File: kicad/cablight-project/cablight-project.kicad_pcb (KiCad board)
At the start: 2 copper layers, 150 x 42 mm, 20 parts, among them J1 Screw_Term_1x2_2.54mm, J2 Screw_Term_1x2_2.54mm, M3 MountingHole_3.2mm_M3_ISO1458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, P1 POLOLU D24V10F5, Q1 IRLB8721PBF, SW1 PEC11, SW3 switch_SPDT_SLW_121586

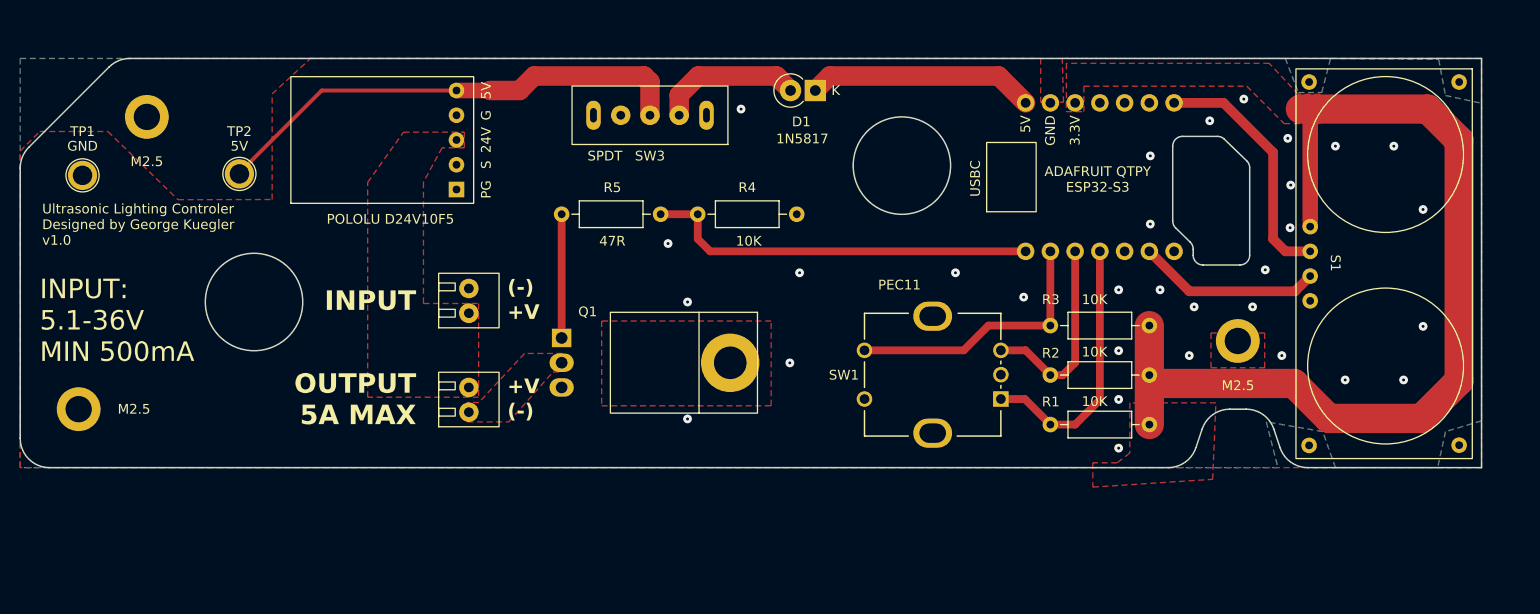
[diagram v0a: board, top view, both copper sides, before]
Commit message: Add Button code support and make ultrasonic notify from task.
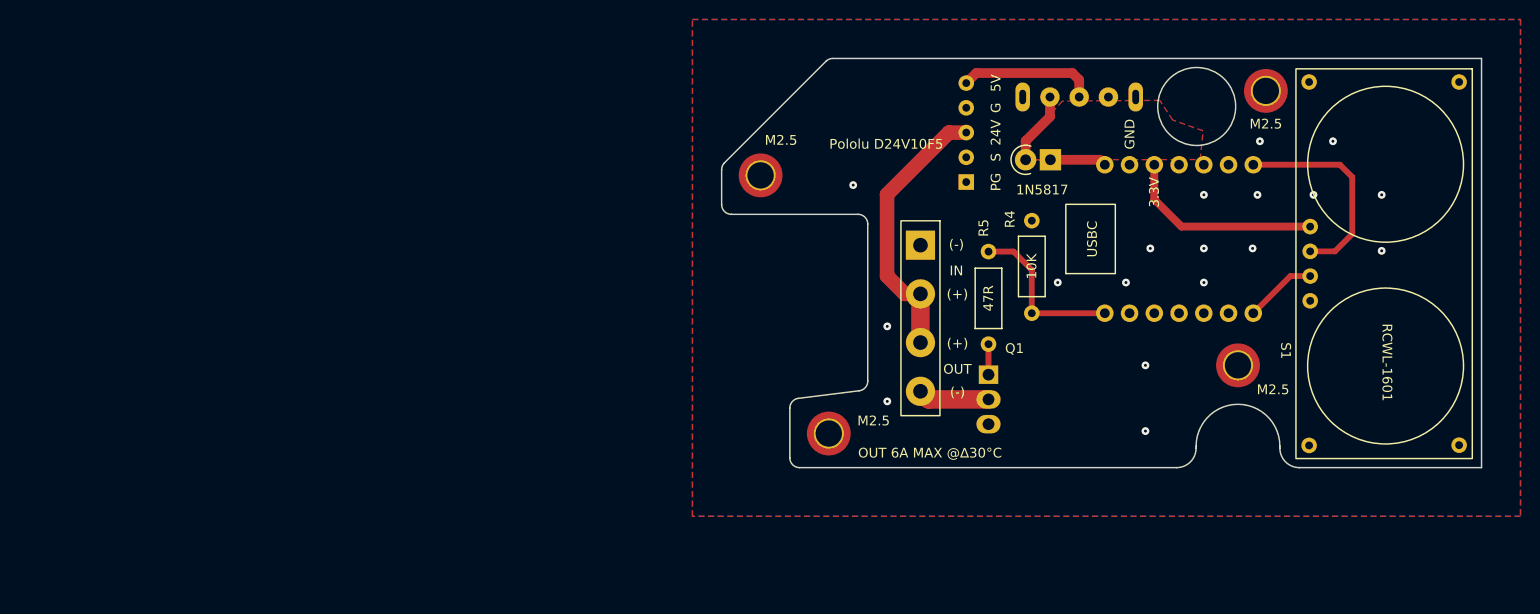
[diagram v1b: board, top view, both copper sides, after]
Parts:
- removed J1, J2: Screw_Term_1x2_2.54mm, user:2xTermBlock_254mm
- removed M3: MountingHole_3.2mm_M3_ISO14580_Pad_TopOnly, user:MountingHole_3.2mm_M3_ISO14580_Pad_TopOnly
- removed R1, R2, R3: 10K, Resistor_THT:R_Axial_DIN0207_L6.3mm_D2.5mm_P10.16mm_Horizontal
- removed REF** (x3): MountingHole_2.7mm_M2.5_ISO7380_Pad_Heated_Insert, user:MountingHole_2.7mm_M2.5_ISO7380_Pad_Heated_Insert
- removed SW1: PEC11, user:Bourns-PEC11R
- removed TP1: GND, TestPoint:TestPoint_Plated_Hole_D2.0mm
- removed TP2: 5V, TestPoint:TestPoint_Plated_Hole_D2.0mm
- added J3: Screw_Term_1x4_5mm, GRK_Lib:Molex 4pin Terminal Block, F.Cu at (-57.6, 19.2)
- added M2.5: MountingHole_2.7mm_M2.5_ISO7380_Pad_TopOnly, MountingHole:MountingHole_2.7mm_M2.5_ISO7380_Pad_TopOnly, F.Cu at (-67.0, 38.5)
- added M2.5: MountingHole_2.7mm_M2.5_ISO7380_Pad_TopOnly, MountingHole:MountingHole_2.7mm_M2.5_ISO7380_Pad_TopOnly, F.Cu at (-25.0, 31.5)
- added M2.5: MountingHole_2.7mm_M2.5_ISO7380_Pad_TopOnly, MountingHole:MountingHole_2.7mm_M2.5_ISO7380_Pad_TopOnly, F.Cu at (-74.0, 12.0)
- added M2.5: MountingHole_2.7mm_M2.5_ISO7380_Pad_TopOnly, MountingHole:MountingHole_2.7mm_M2.5_ISO7380_Pad_TopOnly, F.Cu at (-22.1, 3.33)
- D1: footprint Diode_THT:D_DO-41_SOD81_P2.54mm_Vertical_KathodeUp -> GRK_Lib:D_DO-41_SOD81_P2.54mm_Vertical_KathodeUp
- P1: value POLOLU D24V10F5 -> Pololu D24V10F5; footprint user:Pololu_5V_H -> GRK_Lib:Pololu_5V_H
- Q1: footprint user:TO-220F-3_H_Heatsink -> GRK_Lib:TO-220F-3_H_Heatsink
- R4, R5: footprint Resistor_THT:R_Axial_DIN0207_L6.3mm_D2.5mm_P10.16mm_Horizontal -> GRK_Lib:R_Axial_DIN0207_L6.3mm_D2.5mm_P9.5mm
- S1: footprint user:RCWL-1601 -> GRK_Lib:RCWL-1601
- SW3: footprint user:CUI_SPDT_500mA_3mm -> GRK_Lib:Switch_SPDT_CUI_500mA_3mm
- U1: footprint user:AdafruitQTPyEsp32S3 -> GRK_Lib:AdafruitQTPyEsp32S3
- moved P1 52.3 mm to (-52.9, 7.61)
- moved SW3 44.1 mm to (-41.3, 3.96), turned to 0 degrees
- moved Q1 44.0 mm to (-50.6, 32.5)
- moved R4 35.8 mm to (-46.2, 26.1), turned to 90 degrees
- moved R5 33.9 mm to (-50.6, 19.8), turned to -90 degrees
- moved D1 25.2 mm to (-44.3, 10.4)
- moved U1 10.3 mm to (-38.7, 26.1)
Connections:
- net /+3V3 renamed /SRO4 PWR
- net /+5V_MCU renamed /5V_MCU
- net /+5V_SW renamed /5V_sw
- net Net-(S1-Trig) renamed /trig
- S1 pad 3: Net-(S1-Echo) -> /echo
- U1 pad 2: Net-(SW1-S2) -> unconnected-(U1-GPIO_17-Pad2)
- U1 pad 3: Net-(U1-GPIO_9) -> unconnected-(U1-GPIO_9-Pad3)
- U1 pad 4: Net-(U1-GPIO_8) -> unconnected-(U1-GPIO_8-Pad4)
- U1 pad 6: Net-(S1-Echo) -> unconnected-(U1-GPIO_6-Pad6)
- U1 pad 7: unconnected-(U1-GPIO_5-Pad7) -> /echo
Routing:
- net /SRO4 PWR: track 99.8 -> 20.7 mm
- net /+5V: track 50.1 -> 14.1 mm
- net /+24V: track 0.01 -> 28.3 mm
- net Net-(SW1-S2): track 27.8 -> 0.00 mm
- net Net-(U1-GPIO_8): track 27.5 -> 0.00 mm
- net Net-(U1-GPIO_18): track 40.5 -> 17.2 mm
- net Net-(U1-GPIO_9): track 20.6 -> 0.00 mm
- net Net-(S1-Echo): track 18.9 -> 0.00 mm
- net /5V_MCU: track 23.4 -> 5.80 mm
- net Net-(Q1-G): track 12.7 -> 3.14 mm
- net /5V_sw: track 15.0 -> 7.48 mm
- net /echo: track 0.00 -> 7.42 mm
- net /LED-: track 0.00 -> 7.33 mm
- net /trig: track 25.6 -> 21.6 mm
- net <NO NET>: vias 31 -> 18
- removed copper zone on F.Cu, net /+24V
- removed copper zone on F.Cu, net /LED-
- removed copper zone on F.Cu, net /SRO4 PWR
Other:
- board size 150 x 42 mm -> 78 x 42 mm
- board text added: "(+)"
- board text added: "- Need to confirm my dimensions on the ultrasonic ended up corrent or if I need to adjust tolerences due to soldering error. - Need to attempt to install my M2.5 bosses."
- board text added: "IN"
- board text added: "OUT"
- board text added: "OUT 6A MAX @∆30°C"
- board text added: "Ultrasonic Lighting Controler Designed by George R. Kuegler v2.0 - 2025-07-07 Haverhill, MA"
- board text removed: "+V"
- board text removed: "ADAFRUIT QTPY ESP32-S3"
- board text removed: "Hole for Case Mount"
- board text removed: "INPUT"
- board text removed: "INPUT: 5.1-36V MIN 500mA"
- board text removed: "JLCJLCJLCJLCJLC"
- board text removed: "OUTPUT 5A MAX"
- board text removed: "Ultrasonic Lighting Controler Designed by George Kuegler v1.0"

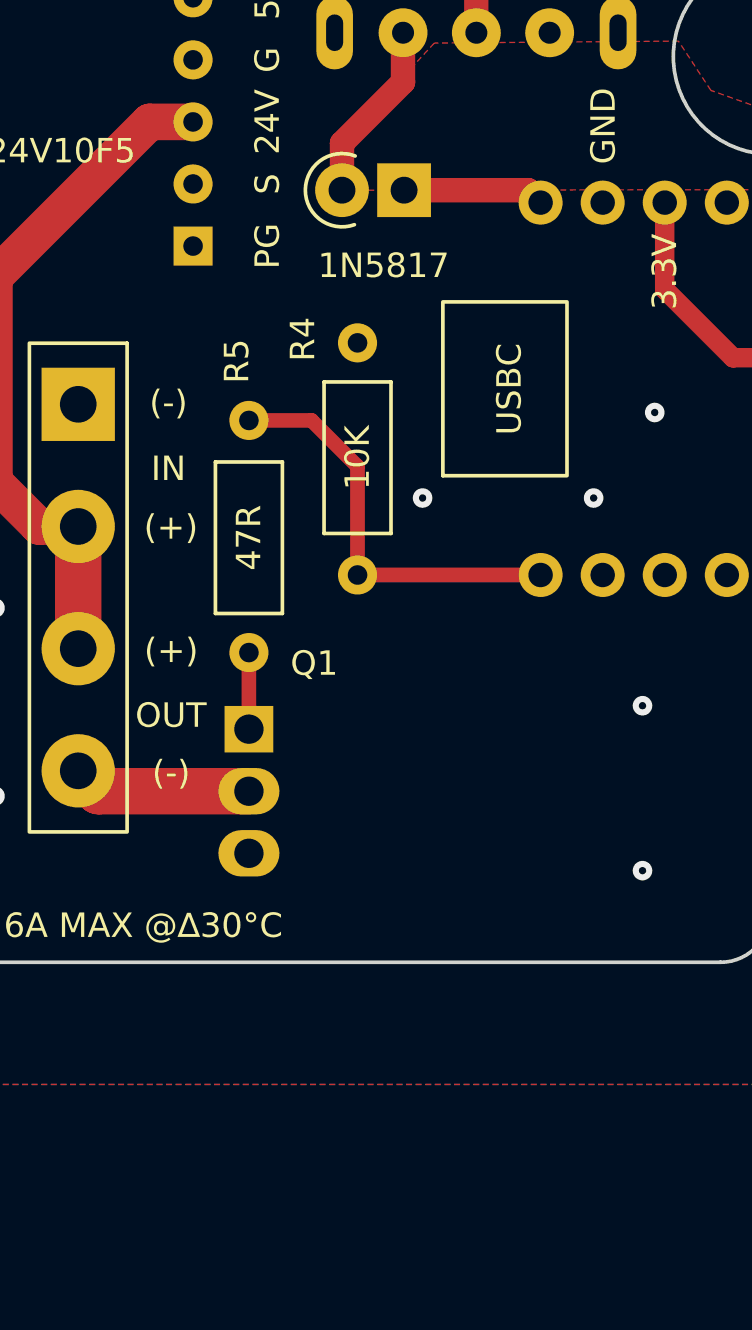
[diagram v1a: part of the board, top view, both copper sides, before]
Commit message: add DIP switch to kicad
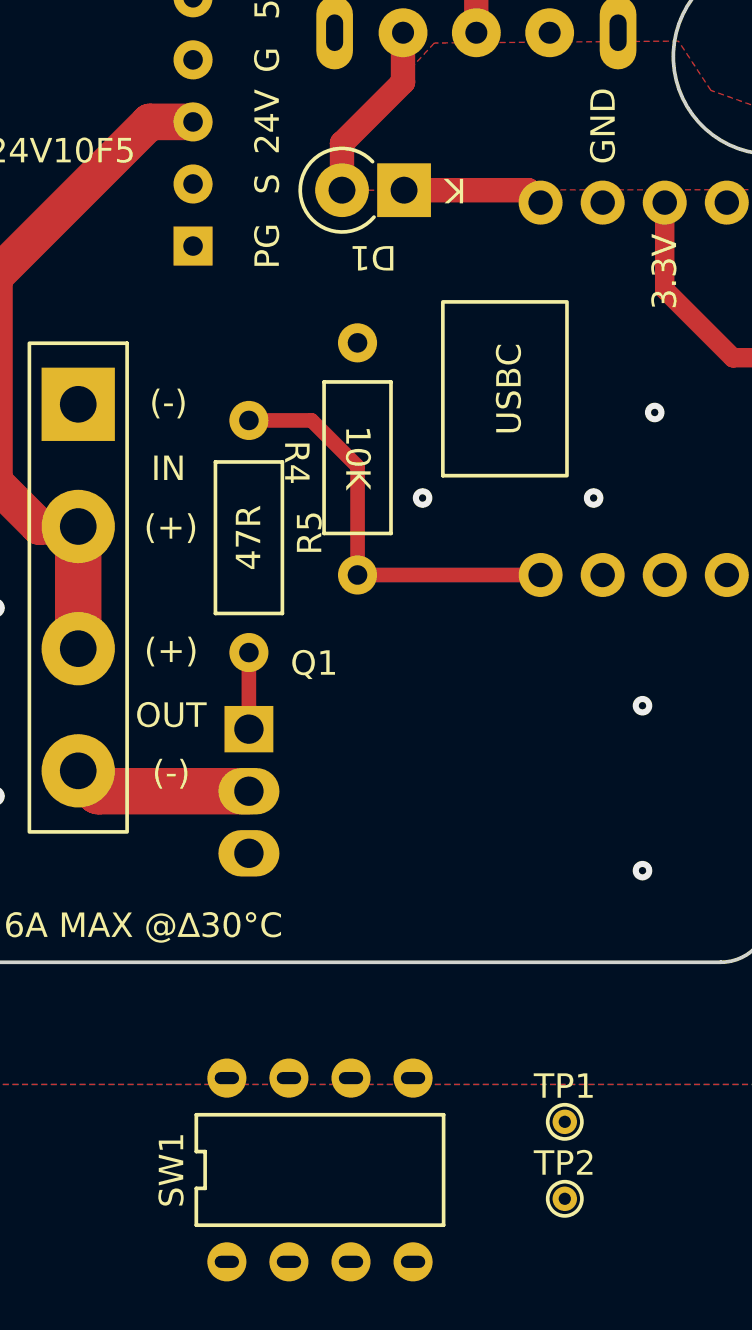
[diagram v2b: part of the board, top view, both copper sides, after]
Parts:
- added SW1: SW_DIP_x04, GRK_Lib:DIP-4 DS04-254 SAME SKY, F.Cu at (-47.7, 50.5)
- added TP1: GND, TestPoint:TestPoint_THTPad_D1.0mm_Drill0.5mm, F.Cu at (-37.7, 48.5)
- added TP2: 5V, TestPoint:TestPoint_THTPad_D1.0mm_Drill0.5mm, F.Cu at (-37.7, 51.7)
- D1: footprint GRK_Lib:D_DO-41_SOD81_P2.54mm_Vertical_KathodeUp -> Diode_THT:D_DO-41_SOD81_P2.54mm_Vertical_KathodeUp
- R4, R5: footprint GRK_Lib:R_Axial_DIN0207_L6.3mm_D2.5mm_P9.5mm -> Resistor_THT:R_Axial_DIN0207_L6.3mm_D2.5mm_P9.5mm
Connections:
- U1 pad 2: unconnected-(U1-GPIO_17-Pad2) -> Net-(U1-GPIO_17)
- U1 pad 3: unconnected-(U1-GPIO_9-Pad3) -> Net-(U1-GPIO_9)
- U1 pad 4: unconnected-(U1-GPIO_8-Pad4) -> Net-(U1-GPIO_8)
- U1 pad 5: unconnected-(U1-GPIO_7-Pad5) -> Net-(U1-GPIO_7)
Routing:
- net Net-(U1-GPIO_8): vias 0 -> 1
- net <NO NET>: vias 18 -> 17
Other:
- board text added: "- put Q1 on reverse side ov board with DIP switches on top? can I put power supply on backside? - downside switch? - conver to smd resistors on backside?"

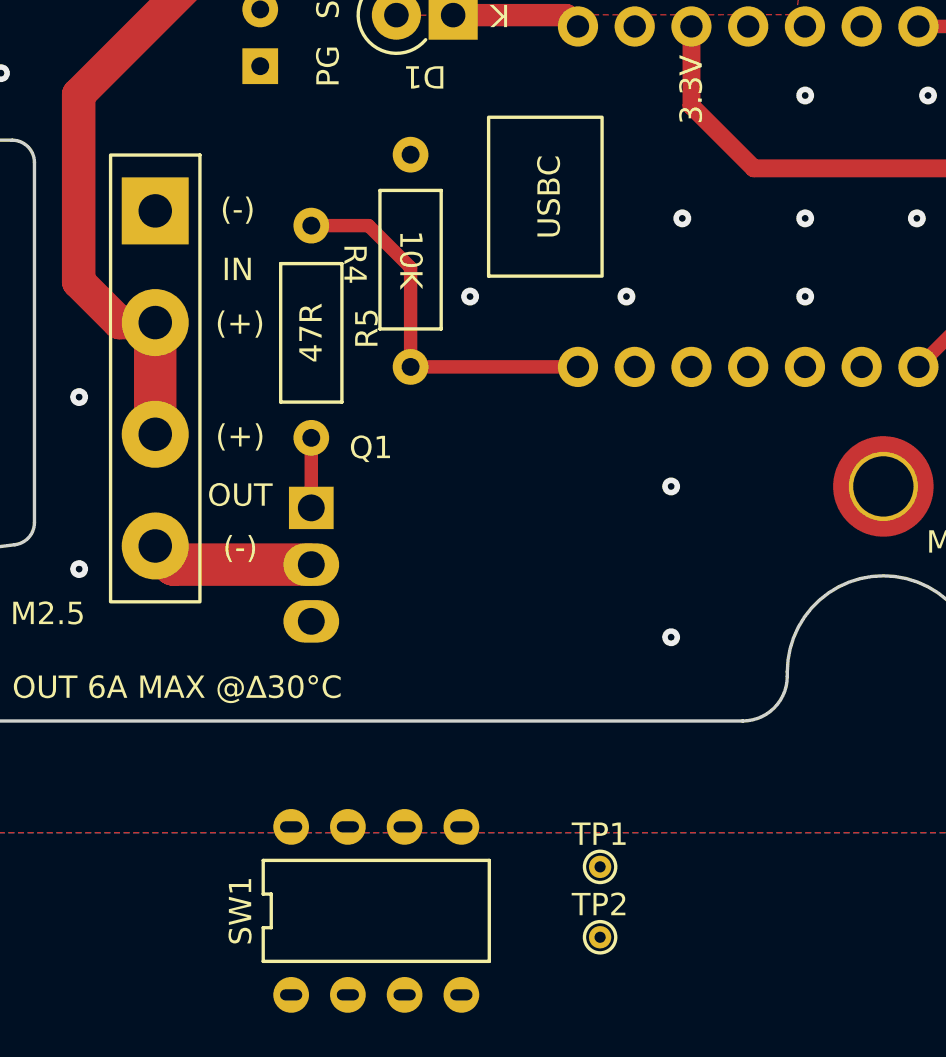
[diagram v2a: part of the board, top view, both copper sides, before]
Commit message: flip Q1 and rotate
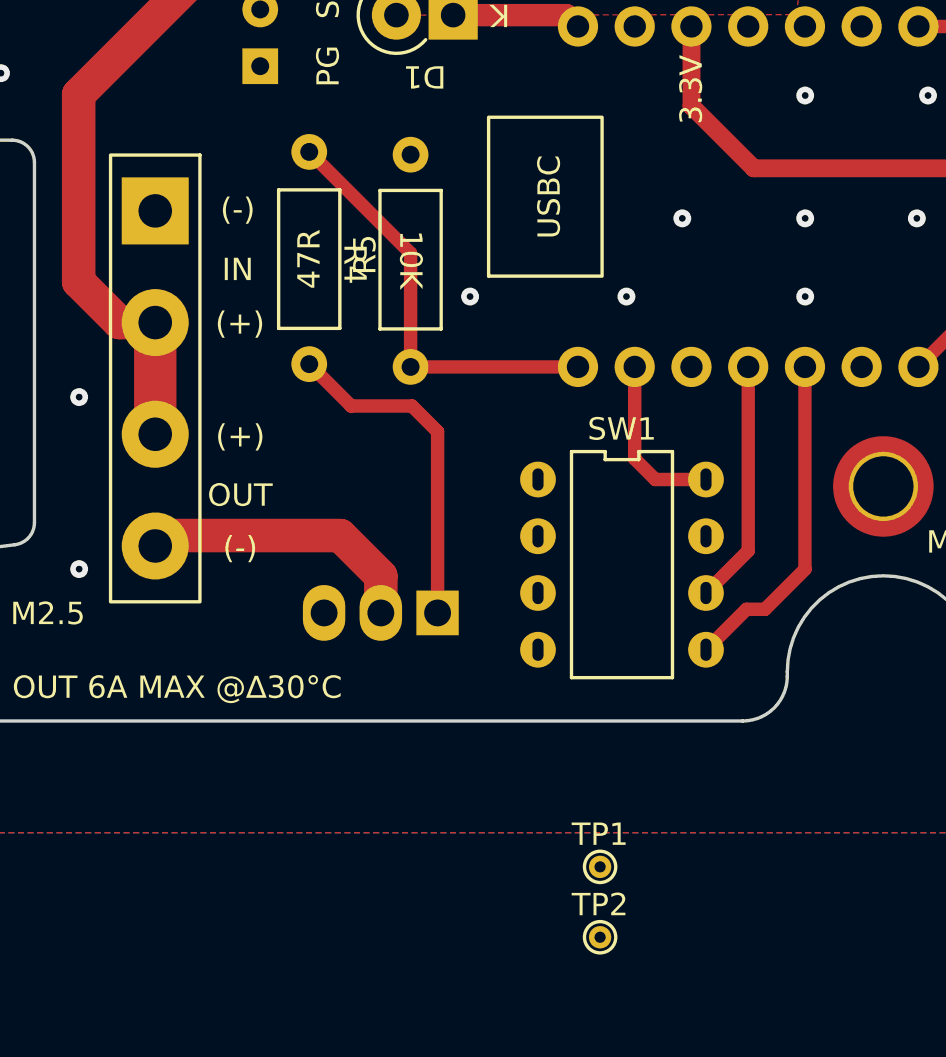
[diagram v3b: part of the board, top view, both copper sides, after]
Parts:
- Q1: moved to B.Cu
- moved SW1 19.0 mm to (-36.7, 35.0), turned to -90 degrees
- moved Q1 7.35 mm to (-45.0, 37.2), turned to 180 degrees
- moved R5 3.30 mm to (-50.7, 16.5)
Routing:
- net Net-(U1-GPIO_7): track 0.00 -> 15.0 mm
- net Net-(Q1-G): track 3.14 -> 15.1 mm
- net Net-(U1-GPIO_8): track 0.00 -> 10.9 mm, vias 1 -> 0
- net Net-(U1-GPIO_17): track 0.00 -> 7.69 mm
- net /LED-: track 7.33 -> 12.7 mm
- net Net-(U1-GPIO_18): track 17.2 -> 19.0 mm
- net <NO NET>: vias 17 -> 16

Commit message: progress
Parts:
- added BTN1: SW_Push, GRK_Lib:Tactile Switch Wurth, F.Cu at (-75.1, 14.6)
- added R1: 10k, Resistor_SMD:R_0805_2012Metric_Pad1.20x1.40mm_HandSolder, F.Cu at (-69.0, 24.1)
- moved M2.5 8.80 mm to (-66.9, 17.2)
- moved J3 2.96 mm to (-57.4, 22.1)
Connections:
- U1 pad 11: unconnected-(U1-GPIO_35-Pad11) -> Net-(U1-GPIO_35)
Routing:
- net /LED-: track 12.7 -> 4.21 mm
- net /+24V: track 28.3 -> 23.3 mm
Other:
- outline, holes or cut-outs redrawn

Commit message: final v1
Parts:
- removed TP1: GND, TestPoint:TestPoint_THTPad_D1.0mm_Drill0.5mm
- removed TP2: 5V, TestPoint:TestPoint_THTPad_D1.0mm_Drill0.5mm
- Q1: moved to F.Cu
- R1: moved to B.Cu
- R4, R5: footprint Resistor_THT:R_Axial_DIN0207_L6.3mm_D2.5mm_P9.5mm -> Resistor_SMD:R_0805_2012Metric_Pad1.20x1.40mm_HandSolder; moved to B.Cu
- moved R1 13.7 mm to (-63.9, 11.4), turned to 180 degrees
- moved R5 10.9 mm to (-52.8, 27.2)
- moved Q1 7.93 mm to (-52.8, 38.3), turned to 0 degrees
- moved J3 4.30 mm to (-61.7, 22.0)
- moved M2.5 3.21 mm to (-70.2, 38.3)
- moved BTN1 2.96 mm to (-74.1, 11.8)
- moved P1 1.89 mm to (-51.0, 7.62)
- moved R4 1.09 mm to (-46.7, 25.2)
- moved SW1 0.49 mm to (-36.3, 34.8), turned to 0 degrees
- moved M2.5 0.20 mm to (-66.9, 17.4)
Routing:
- net Net-(U1-GPIO_35): track 0.00 -> 53.1 mm, vias 0 -> 3
- net /SRO4 PWR: track 20.7 -> 52.6 mm, vias 0 -> 1
- net /LED-: track 4.21 -> 15.9 mm
- net /+24V: track 23.3 -> 33.2 mm
- net Net-(U1-GPIO_7): track 15.0 -> 7.70 mm
- net Net-(U1-GPIO_9): track 0.00 -> 6.81 mm
- net Net-(Q1-G): track 15.1 -> 10.1 mm
- net Net-(U1-GPIO_18): track 19.0 -> 14.2 mm
- net Net-(U1-GPIO_8): track 10.9 -> 8.01 mm
- net /+5V: track 14.1 -> 12.2 mm
- net Net-(U1-GPIO_17): track 7.69 -> 6.49 mm
- net <NO NET>: vias 16 -> 17
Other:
- board size 78 x 42 mm -> 75.5 x 42 mm
- board text removed: "- Need to confirm my dimensions on the ultrasonic ended up corrent or if I need to adjust tolerences due to soldering error. - Need to attempt to install my M2.5 bosses."
- board text removed: "- put Q1 on reverse side ov board with DIP switches on top? can I put power supply on backside? - downside switch? - conver to smd resistors on backside?"
